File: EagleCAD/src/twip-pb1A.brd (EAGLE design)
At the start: 126.7 x 82.5 mm, 23 parts, among them J1 UJ2-BH-1-TH

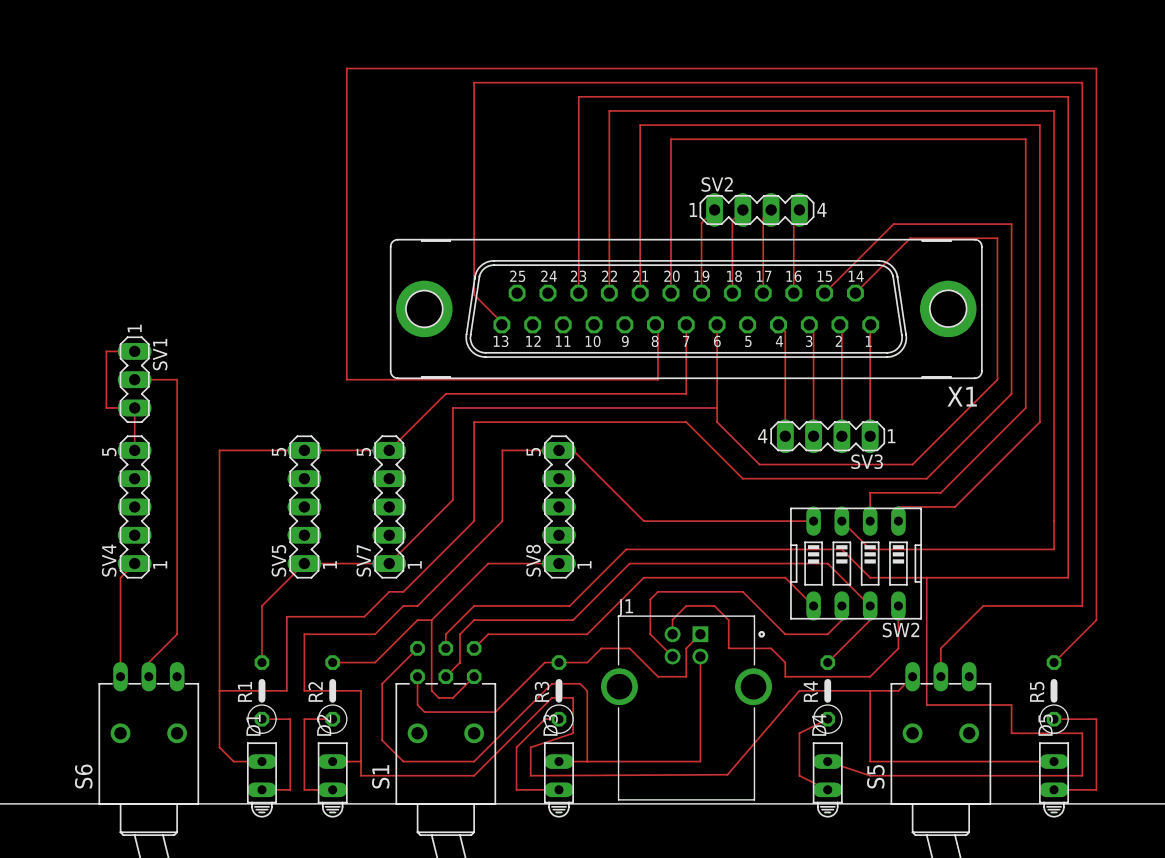
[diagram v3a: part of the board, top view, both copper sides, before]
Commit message: widen all traces from .006 to .012 inch
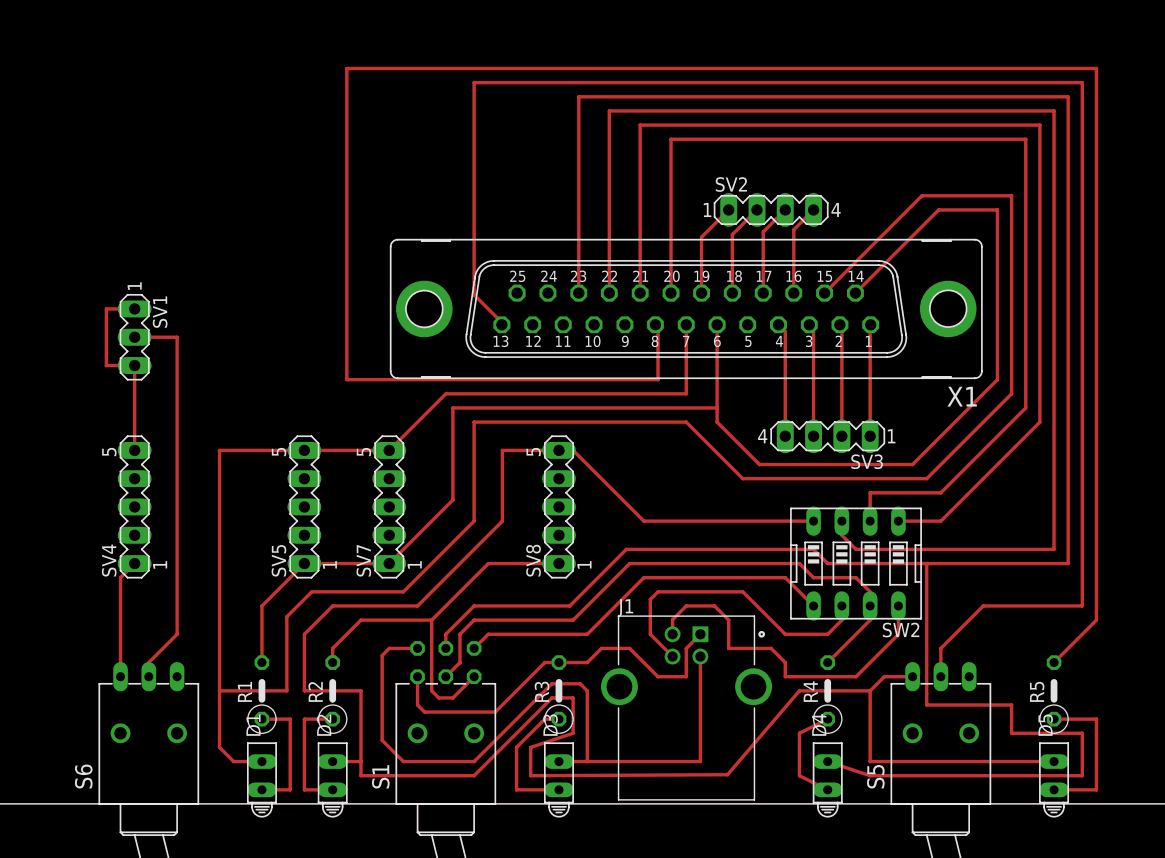
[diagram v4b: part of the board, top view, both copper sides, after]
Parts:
- moved SV1 3.81 mm to (11.4, 73.7)
- moved SV2 1.27 mm to (68.6, 85.1)
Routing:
- net N$7: track 31.5 -> 35.3 mm
- net N$6: track 14.0 -> 17.8 mm
- net N$8: track 124.3 -> 127.9 mm
- net N$29: track 211.3 -> 214.9 mm
- net N$23: track 60.4 -> 61.9 mm
- net N$24: track 94.8 -> 94.0 mm
- net N$22: track 52.1 -> 52.8 mm
- net N$13: track 31.8 -> 31.1 mm
- net N$12: track 35.2 -> 36.0 mm
- net N$25: track 115.8 -> 116.5 mm
- net N$18: track 7.86 -> 8.38 mm
- net N$27: track 220.9 -> 220.4 mm
- net N$20: track 7.68 -> 8.20 mm
- net N$11: track 7.95 -> 8.48 mm
- net N$19: track 7.76 -> 8.29 mm
